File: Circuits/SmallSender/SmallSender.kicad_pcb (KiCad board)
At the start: 2 copper layers, 28 x 49.6 mm, 11 parts, among them P1 WRITER-VCC, SW1 SPST, SW2 FR2S1015, SW3 SKRPACE010, U1 TWE_LITE_SMD, U2 HN2S01FU

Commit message: Added drill center hole.
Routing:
- net /ExtVcc: track 70.9 -> 78.5 mm
- net /DI1: track 46.2 -> 50.8 mm
- net GND: track 120.2 -> 122.1 mm
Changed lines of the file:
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@@
     (thickness 1)
     (drawings 2)
-    (tracks 222)
+    (tracks 226)
     (zones 0)
     (modules 11)
@@
     )
   )
-  (module favorites:B3FS-4002P (layer F.Cu)
-    (at 30 31)
-    (fp_text reference SW1 (at 0 -1.3335) (layer F.SilkS)
-      (effects (font (size 1 1) (thickness 0.15)))
-    )
-    (fp_text value SPST (at 0 0) (layer F.SilkS) hide
-      (effects (font (size 1 1) (thickness 0.15)))
-    )
-    (fp_line (start -6.096 6.096) (end 6.096 6.096) (layer Dwgs.User) (width 0.15))
-    (fp_line (start 6.096 -6.096) (end 6.096 6.096) (layer Dwgs.User) (width 0.15))
-    (fp_line (start 6.096 -6.096) (end -6.096 -6.096) (layer Dwgs.User) (width 0.15))
-    (fp_line (start -6.096 -6.096) (end -6.096 6.096) (layer Dwgs.User) (width 0.15))
-    (pad 1 smd rect (at 7.15 2.5) (size 2.3 1.2) (layers F.Cu F.Paste F.Mask)
-      (net 3 /DI1))
-    (pad 1 smd rect (at -7.15 2.5) (size 2.3 1.2) (layers F.Cu F.Paste F.Mask)
-      (net 3 /DI1))
-    (pad 2 smd rect (at 7.15 -2.5) (size 2.3 1.2) (layers F.Cu F.Paste F.Mask)
-      (net 11 GND))
-    (pad 2 smd rect (at -7.15 -2.5) (size 2.3 1.2) (layers F.Cu F.Paste F.Mask)
-      (net 11 GND))
-    (model favorites/B3FS-4002P.wrl
-      (at (xyz 0 0 0))
-      (scale (xyz 0.393701 0.393701 0.393701))
-      (rotate (xyz 0 0 0))
-    )
-  )
   (module favorites:TWE-001L-NC7 (layer B.Cu)
     (at 30 49 180)
@@
     )
   )
+  (module favorites:B3FS-4002P (layer F.Cu)
+    (at 30 31)
+    (fp_text reference SW1 (at 0 -1.9) (layer F.SilkS)
+      (effects (font (size 1 1) (thickness 0.15)))
+    )
+    (fp_text value SPST (at 0 1.8) (layer F.SilkS) hide
+      (effects (font (size 1 1) (thickness 0.15)))
+    )
+    (fp_line (start -6.096 6.096) (end 6.096 6.096) (layer Dwgs.User) (width 0.15))
+    (fp_line (start 6.096 -6.096) (end 6.096 6.096) (layer Dwgs.User) (width 0.15))
+    (fp_line (start 6.096 -6.096) (end -6.096 -6.096) (layer Dwgs.User) (width 0.15))
+    (fp_line (start -6.096 -6.096) (end -6.096 6.096) (layer Dwgs.User) (width 0.15))
+    (pad 1 smd rect (at 7.15 2.5) (size 2.3 1.2) (layers F.Cu F.Paste F.Mask)
+      (net 3 /DI1))
+    (pad 1 smd rect (at -7.15 2.5) (size 2.3 1.2) (layers F.Cu F.Paste F.Mask)
+      (net 3 /DI1))
+    (pad 2 smd rect (at 7.15 -2.5) (size 2.3 1.2) (layers F.Cu F.Paste F.Mask)
+      (net 11 GND))
+    (pad 2 smd rect (at -7.15 -2.5) (size 2.3 1.2) (layers F.Cu F.Paste F.Mask)
+      (net 11 GND))
+    (pad "" np_thru_hole circle (at 0 0) (size 2 2) (drill 2) (layers *.Cu *.Mask F.SilkS))
+    (model favorites/B3FS-4002P.wrl
+      (at (xyz 0 0 0))
+      (scale (xyz 0.393701 0.393701 0.393701))
+      (rotate (xyz 0 0 0))
+    )
+  )
   (gr_text CR2032 (at 30 60) (layer F.SilkS)
     (effects (font (size 1.5 1.5) (thickness 0.3)))
@@
   (segment (start 30.1034 57.3229) (end 24.5998 57.3229) (width 0.254) (layer B.Cu) (net 2))
   (segment (start 30.635 56.7913) (end 30.1034 57.3229) (width 0.254) (layer B.Cu) (net 2))
+  (segment (start 37.15 33.5) (end 37.15 34.351) (width 0.254) (layer F.Cu) (net 3))
+  (segment (start 24.1655 33.5) (end 22.85 33.5) (width 0.254) (layer F.Cu) (net 3))
+  (segment (start 28.5115 37.846) (end 24.1655 33.5) (width 0.254) (layer F.Cu) (net 3))
+  (segment (start 33.655 37.846) (end 28.5115 37.846) (width 0.254) (layer F.Cu) (net 3))
+  (segment (start 37.15 34.351) (end 33.655 37.846) (width 0.254) (layer F.Cu) (net 3))
   (via (at 21.5413 54.511) (size 0.889) (layers F.Cu B.Cu) (net 3))
-  (segment (start 37.15 33.5) (end 35.6437 33.5) (width 0.254) (layer F.Cu) (net 3))
-  (segment (start 24.3563 33.5) (end 35.6437 33.5) (width 0.254) (layer F.Cu) (net 3))
   (segment (start 22.85 33.5) (end 23.4032 33.5) (width 0.254) (layer F.Cu) (net 3))
-  (segment (start 23.4032 33.5) (end 24.3563 33.5) (width 0.254) (layer F.Cu) (net 3))
   (segment (start 29.365 55.735) (end 29.365 56.7913) (width 0.254) (layer B.Cu) (net 3))
   (segment (start 21.5413 35.3619) (end 23.4032 33.5) (width 0.254) (layer F.Cu) (net 3))
@@
   (segment (start 30.89 57.8063) (end 24.3997 57.8063) (width 0.254) (layer B.Cu) (net 5))
   (segment (start 31.905 56.7913) (end 30.89 57.8063) (width 0.254) (layer B.Cu) (net 5))
+  (segment (start 18.5 33.5) (end 18.5 33.74) (width 0.254) (layer B.Cu) (net 6))
+  (segment (start 18.5 33.74) (end 23.3045 38.5445) (width 0.254) (layer B.Cu) (net 6))
   (via (at 37.4755 42.857) (size 0.889) (layers F.Cu B.Cu) (net 6))
   (via (at 37.934 40.7833) (size 0.889) (layers F.Cu B.Cu) (net 6))
@@
   (segment (start 37.7913 43.1728) (end 37.4755 42.857) (width 0.254) (layer B.Cu) (net 6))
   (segment (start 37.7913 45.825) (end 37.7913 43.1728) (width 0.254) (layer B.Cu) (net 6))
-  (segment (start 30.6507 33.5) (end 37.934 40.7833) (width 0.254) (layer B.Cu) (net 6))
-  (segment (start 18.5 33.5) (end 30.6507 33.5) (width 0.254) (layer B.Cu) (net 6))
+  (segment (start 35.6952 38.5445) (end 37.934 40.7833) (width 0.254) (layer B.Cu) (net 6))
+  (segment (start 23.3045 38.5445) (end 35.6952 38.5445) (width 0.254) (layer B.Cu) (net 6))
   (segment (start 37.934 42.3985) (end 37.934 40.7833) (width 0.254) (layer F.Cu) (net 6))
   (segment (start 37.4755 42.857) (end 37.934 42.3985) (width 0.254) (layer F.Cu) (net 6))
@@
   (segment (start 35.3148 41.9) (end 35.3148 41.366) (width 0.381) (layer B.Cu) (net 11))
   (segment (start 30 49) (end 32.4198 49) (width 0.381) (layer F.Cu) (net 11))
-  (segment (start 39.2073 28.9875) (end 38.7198 28.5) (width 0.381) (layer F.Cu) (net 11))
-  (segment (start 39.2073 38.9675) (end 39.2073 28.9875) (width 0.381) (layer F.Cu) (net 11))
-  (segment (start 38.3014 39.8734) (end 39.2073 38.9675) (width 0.381) (layer F.Cu) (net 11))
+  (segment (start 41.529 31.3092) (end 38.7198 28.5) (width 0.381) (layer F.Cu) (net 11))
+  (segment (start 41.529 36.6458) (end 41.529 31.3092) (width 0.381) (layer F.Cu) (net 11))
+  (segment (start 38.3014 39.8734) (end 41.529 36.6458) (width 0.381) (layer F.Cu) (net 11))
   (segment (start 36.8074 39.8734) (end 38.3014 39.8734) (width 0.381) (layer F.Cu) (net 11))
   (segment (start 35.6361 41.0447) (end 36.8074 39.8734) (width 0.381) (layer F.Cu) (net 11))
@@
   (segment (start 31.7822 18.8793) (end 31.7822 17.619) (width 0.254) (layer F.Cu) (net 25))
   (segment (start 31.4199 16) (end 31.4199 17.2567) (width 0.254) (layer F.Cu) (net 25))
-  (segment (start 24.2235 25.88) (end 18.5 25.88) (width 0.254) (layer B.Cu) (net 26))
-  (segment (start 38.8006 40.4571) (end 24.2235 25.88) (width 0.254) (layer B.Cu) (net 26))
-  (segment (start 38.8006 41.3049) (end 38.8006 40.4571) (width 0.254) (layer B.Cu) (net 26))
+  (segment (start 37.241 25.88) (end 18.5 25.88) (width 0.254) (layer B.Cu) (net 26))
+  (segment (start 38.8006 27.4396) (end 37.241 25.88) (width 0.254) (layer B.Cu) (net 26))
+  (segment (start 38.8006 41.3049) (end 38.8006 27.4396) (width 0.254) (layer B.Cu) (net 26))
   (segment (start 39.41 41.9143) (end 38.8006 41.3049) (width 0.254) (layer B.Cu) (net 26))
   (segment (start 40.4244 41.9143) (end 39.41 41.9143) (width 0.254) (layer B.Cu) (net 26))
@@
   (segment (start 23.669 60.3498) (end 22.5621 60.3498) (width 0.254) (layer B.Cu) (net 26))
   (via (at 32.8777 40.4392) (size 0.889) (layers F.Cu B.Cu) (net 27))
+  (segment (start 26.825 41.2087) (end 27.5945 40.4392) (width 0.254) (layer B.Cu) (net 27))
+  (segment (start 27.5945 40.4392) (end 32.8777 40.4392) (width 0.254) (layer B.Cu) (net 27))
+  (segment (start 32.9563 22.075) (end 32.9563 26.9984) (width 0.254) (layer F.Cu) (net 27))
+  (segment (start 32.9563 26.9984) (end 38.6564 32.6985) (width 0.254) (layer F.Cu) (net 27))
+  (segment (start 38.6564 32.6985) (end 38.6564 34.6605) (width 0.254) (layer F.Cu) (net 27))
+  (segment (start 38.6564 34.6605) (end 32.8777 40.4392) (width 0.254) (layer F.Cu) (net 27))
+  (segment (start 26.825 42.265) (end 26.825 41.2087) (width 0.254) (layer B.Cu) (net 27))
+  (segment (start 32.075 22.075) (end 32.9563 22.075) (width 0.254) (layer F.Cu) (net 27))
   (segment (start 27.925 22.075) (end 32.075 22.075) (width 0.254) (layer F.Cu) (net 27))
-  (segment (start 32.075 22.075) (end 32.9563 22.075) (width 0.254) (layer F.Cu) (net 27))
-  (segment (start 26.825 42.265) (end 26.825 41.2087) (width 0.254) (layer B.Cu) (net 27))
-  (segment (start 38.6564 34.6605) (end 32.8777 40.4392) (width 0.254) (layer F.Cu) (net 27))
-  (segment (start 38.6564 32.6985) (end 38.6564 34.6605) (width 0.254) (layer F.Cu) (net 27))
-  (segment (start 32.9563 26.9984) (end 38.6564 32.6985) (width 0.254) (layer F.Cu) (net 27))
-  (segment (start 32.9563 22.075) (end 32.9563 26.9984) (width 0.254) (layer F.Cu) (net 27))
-  (segment (start 27.5945 40.4392) (end 32.8777 40.4392) (width 0.254) (layer B.Cu) (net 27))
-  (segment (start 26.825 41.2087) (end 27.5945 40.4392) (width 0.254) (layer B.Cu) (net 27))
   (zone (net 0) (net_name "") (layer B.Cu) (hatch edge 0.508)
     (connect_pads (clearance 0.508))

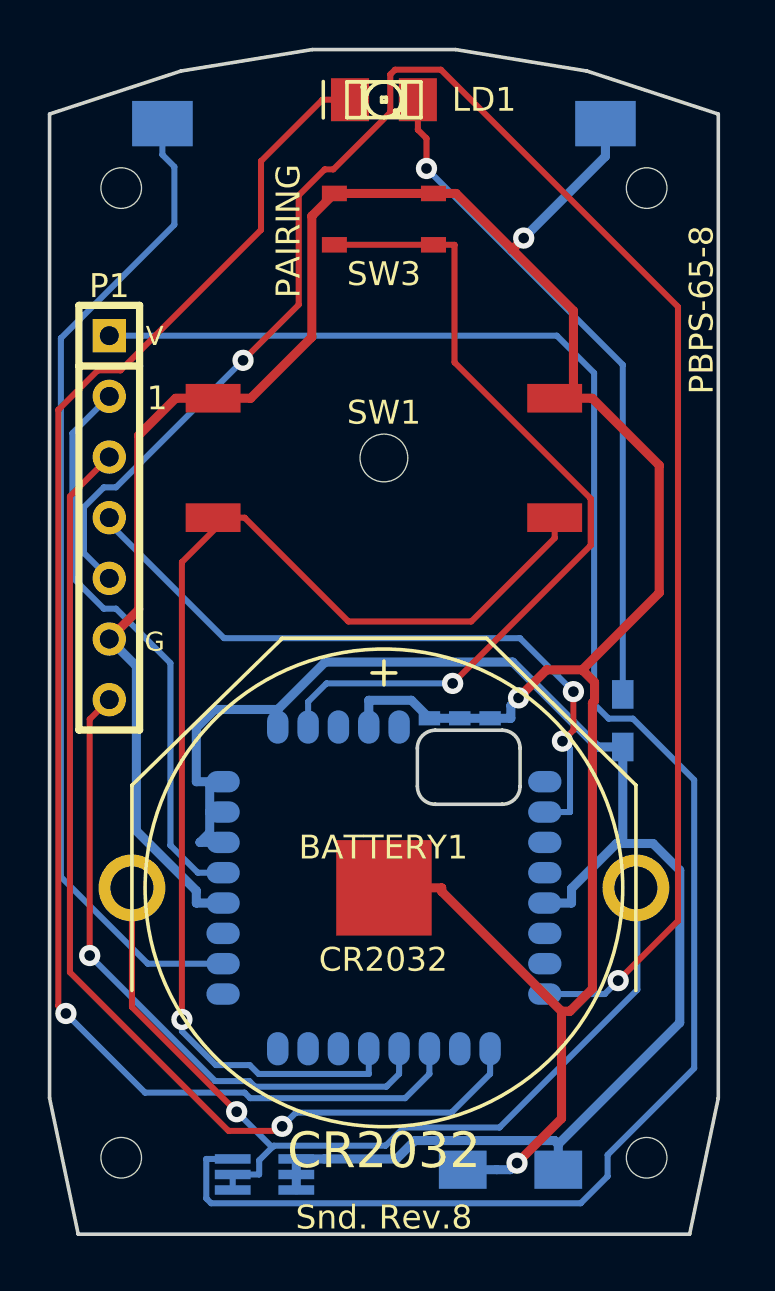
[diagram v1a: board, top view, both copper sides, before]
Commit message: Duplicated trigger tactical switch.
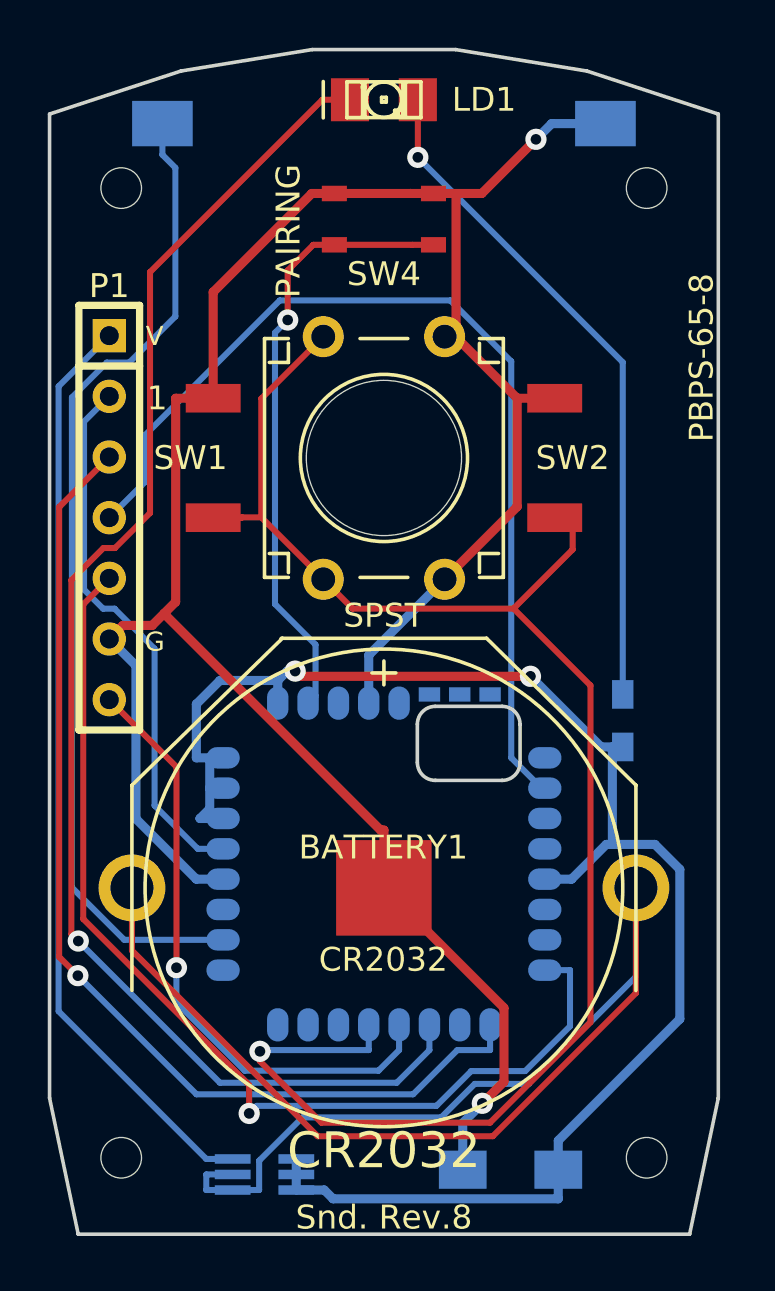
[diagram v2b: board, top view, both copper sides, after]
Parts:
- added SW2: SPST, favorites:JB-15HFBP2, F.Cu at (30.0, 31.0)
- moved U1 1.00 mm to (30.0, 48.0)
- renumbered SW2 to SW3, SW3 to SW4
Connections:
- U1 pad 30: GND -> Net-(U1-Pad30)
- U1 pad 31: GND -> Net-(U1-Pad31)
- U1 pad 32: GND -> Net-(U1-Pad32)
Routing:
- net /ExtVcc: track 78.5 -> 39.0 mm
- net /TXD: track 76.2 -> 44.1 mm, vias 2 -> 1
- net /3V: track 38.7 -> 61.7 mm, vias 1 -> 0
- net /DI1: track 50.8 -> 69.7 mm
- net GND: track 122.1 -> 107.1 mm, vias 3 -> 2
- net /PRG: track 29.0 -> 41.3 mm, vias 2 -> 0
- net /PAIRING: track 35.6 -> 25.7 mm
- net /DO4: track 62.9 -> 59.9 mm
- net /CFG: track 27.6 -> 25.8 mm
- net /RST: track 24.1 -> 22.7 mm
- net /RXD: track 44.6 -> 44.1 mm
- net /Vcc: track 67.7 -> 67.4 mm, vias 0 -> 2

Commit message: Rerouted.
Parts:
- SW1: footprint favorites:B3FS-4002P -> favorites:B3FS-4002P_centerHole2_5mm
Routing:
- net /PRG: track 41.3 -> 26.3 mm
- net GND: track 107.1 -> 119.1 mm
- net /DI1: track 69.7 -> 76.2 mm
- net /3V: track 61.7 -> 63.4 mm
- net /CFG: track 25.8 -> 27.1 mm, vias 1 -> 0
- net /LED: track 28.5 -> 29.6 mm
- net /RXD: track 44.1 -> 43.0 mm
- net /DO4: track 59.9 -> 59.0 mm
- net /DI4: track 41.8 -> 41.5 mm, vias 0 -> 2
- net /TXD: track 44.1 -> 44.2 mm, vias 1 -> 0

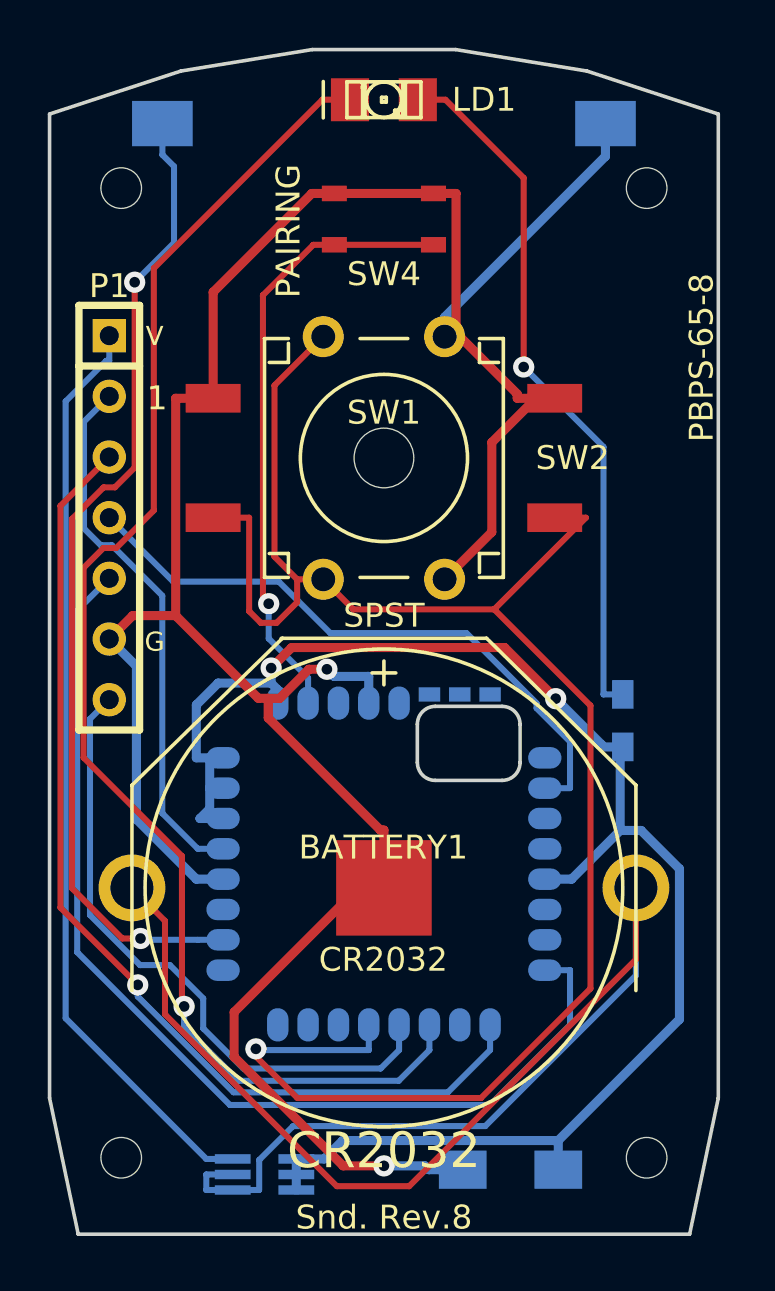
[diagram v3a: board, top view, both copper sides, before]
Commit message: Added voltage detector.
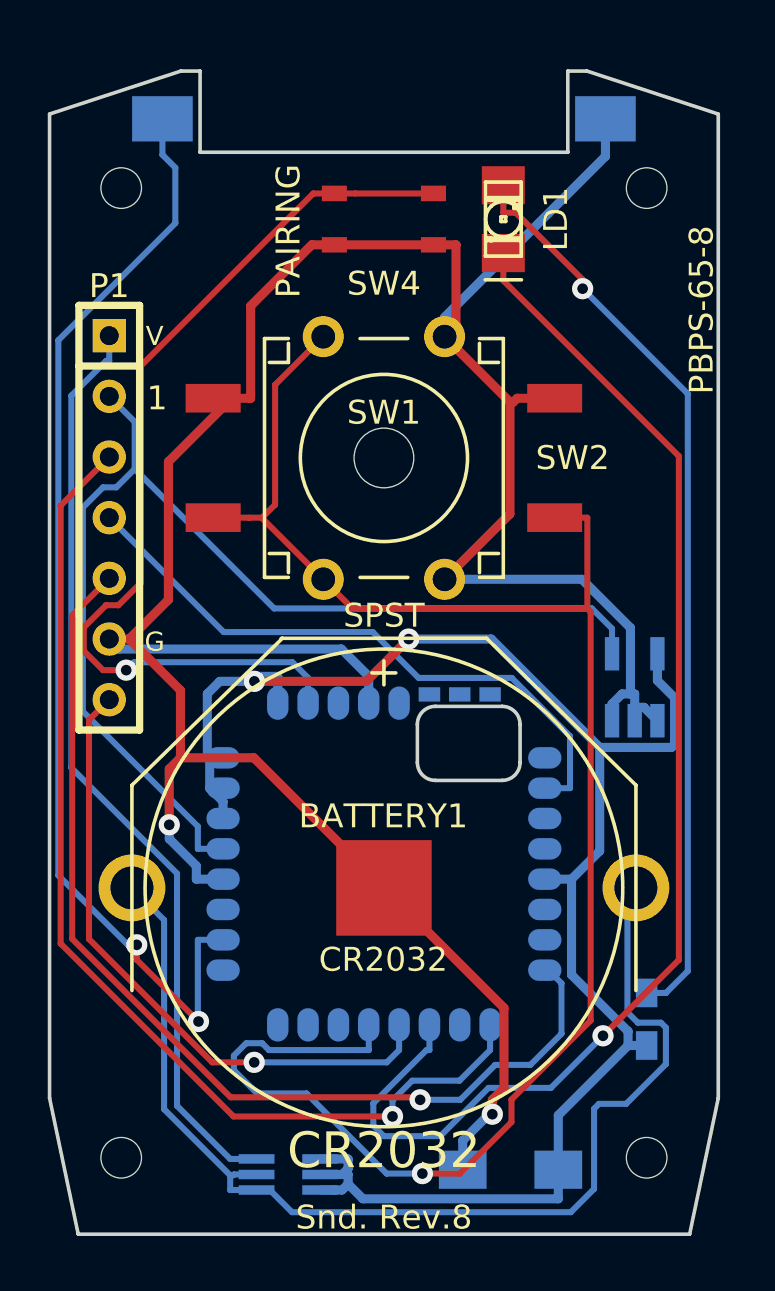
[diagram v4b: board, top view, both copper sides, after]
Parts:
- added U3: BD45231G, favorites:SSOP5_Handsoldering, B.Cu at (40.5, 40.6)
- moved R1 12.5 mm to (41.0, 54.5)
- moved LD1 7.07 mm to (35.0, 21.0), turned to 90 degrees
- moved U2 1.00 mm to (26.0, 61.0)
- moved SW3 0.20 mm to (30.0, 16.8)
- turned SW4 to 0 degrees
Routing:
- net /RST: track 22.7 -> 47.5 mm
- net /3V: track 63.4 -> 47.4 mm
- net /PAIRING: track 25.9 -> 39.7 mm
- net /LED: track 29.6 -> 38.5 mm
- net /DI4: track 41.5 -> 47.0 mm
- net /Vcc: track 67.5 -> 72.6 mm
- net GND: track 119.1 -> 124.2 mm
- net /DO4: track 59.0 -> 53.9 mm
- net /RXD: track 43.0 -> 44.8 mm
- net /TXD: track 44.2 -> 43.2 mm, vias 0 -> 1
- net /CFG: track 27.1 -> 26.8 mm, vias 0 -> 1
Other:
- board size 28 x 49.6 mm -> 28 x 48.7 mm

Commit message: Added a voltage detector.
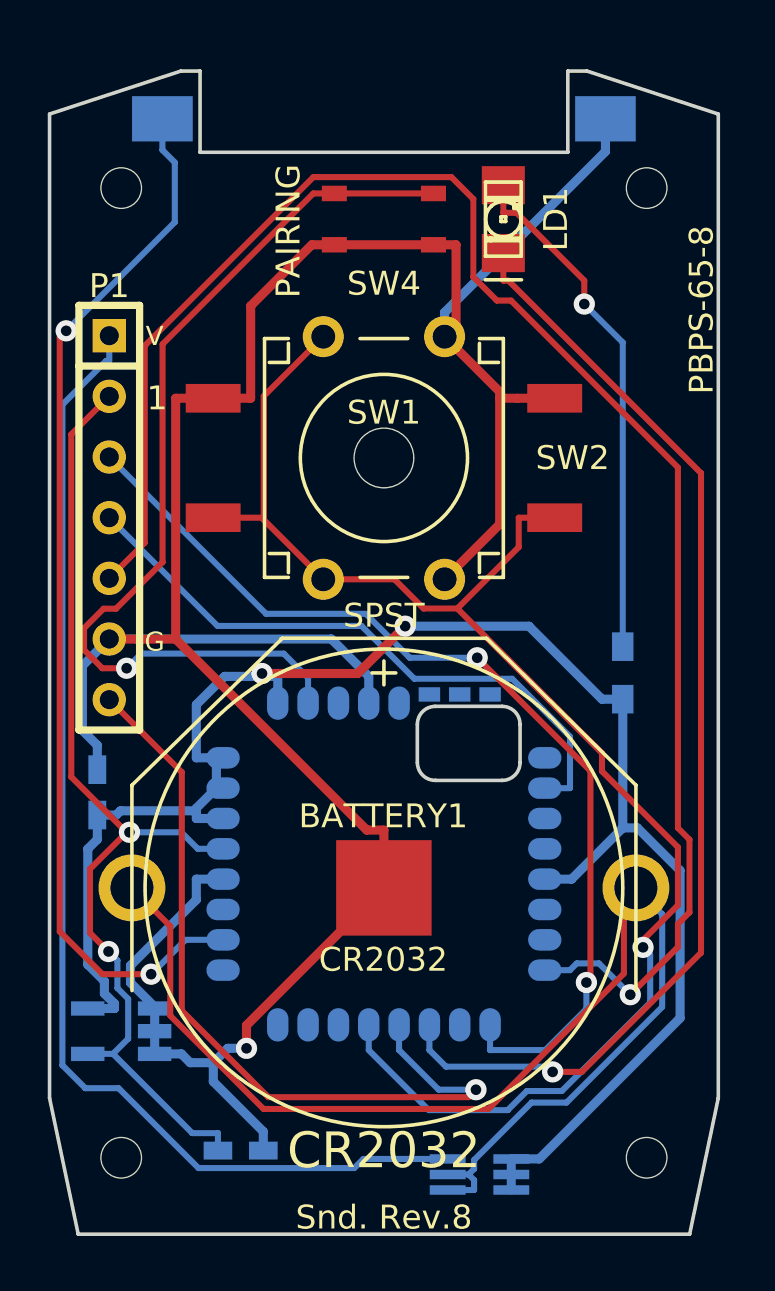
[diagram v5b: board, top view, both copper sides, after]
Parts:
- added C2: 1000p, Capacitors_SMD:C_0603_HandSoldering, B.Cu at (24.0, 60.0)
- C1: value 100u -> 10u; footprint Capacitors_SMD:C_1206_HandSoldering -> Capacitors_SMD:C_0603_HandSoldering
- moved U3 25.9 mm to (19.0, 55.0), turned to 270 degrees
- moved C1 23.4 mm to (18.0, 45.0), turned to 90 degrees
- moved R1 14.5 mm to (40.0, 40.0)
- moved U2 8.00 mm to (34.0, 61.0)
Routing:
- net /TXD: track 43.2 -> 70.1 mm
- net /LED: track 38.5 -> 21.7 mm
- net /DI1: track 76.0 -> 63.6 mm
- net /ExtVcc: track 39.1 -> 49.5 mm
- net /CFG: track 26.8 -> 33.2 mm
- net /DO4: track 53.9 -> 47.7 mm
- net /RST: track 47.5 -> 42.6 mm, vias 0 -> 2
- net /3V: track 47.4 -> 52.2 mm
- net /RXD: track 44.8 -> 41.4 mm, vias 1 -> 2
- net GND: track 124.2 -> 121.0 mm, vias 2 -> 1
- net /DI4: track 47.0 -> 44.4 mm
- net /Vcc: track 72.6 -> 73.8 mm

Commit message: Added 3D shape of a SMD LED.
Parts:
- U2: footprint Housings_SOT-23_SOT-143_TSOT-6:SC-70-6_Handsoldering -> TO_SOT_Packages_SMD:SC-70-6_Handsoldering
